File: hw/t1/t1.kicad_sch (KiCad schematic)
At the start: 62 parts, among them J1 SFP edge (INF-8074i), J2 H-MTD 1-port PCB header - FOO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, U1 DP83TG720S-Q1 (or DP83TC812S-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, U2 STM32G031F6P6, U3 TPS62821DLC, Y1 25MHz CL8pF 2016

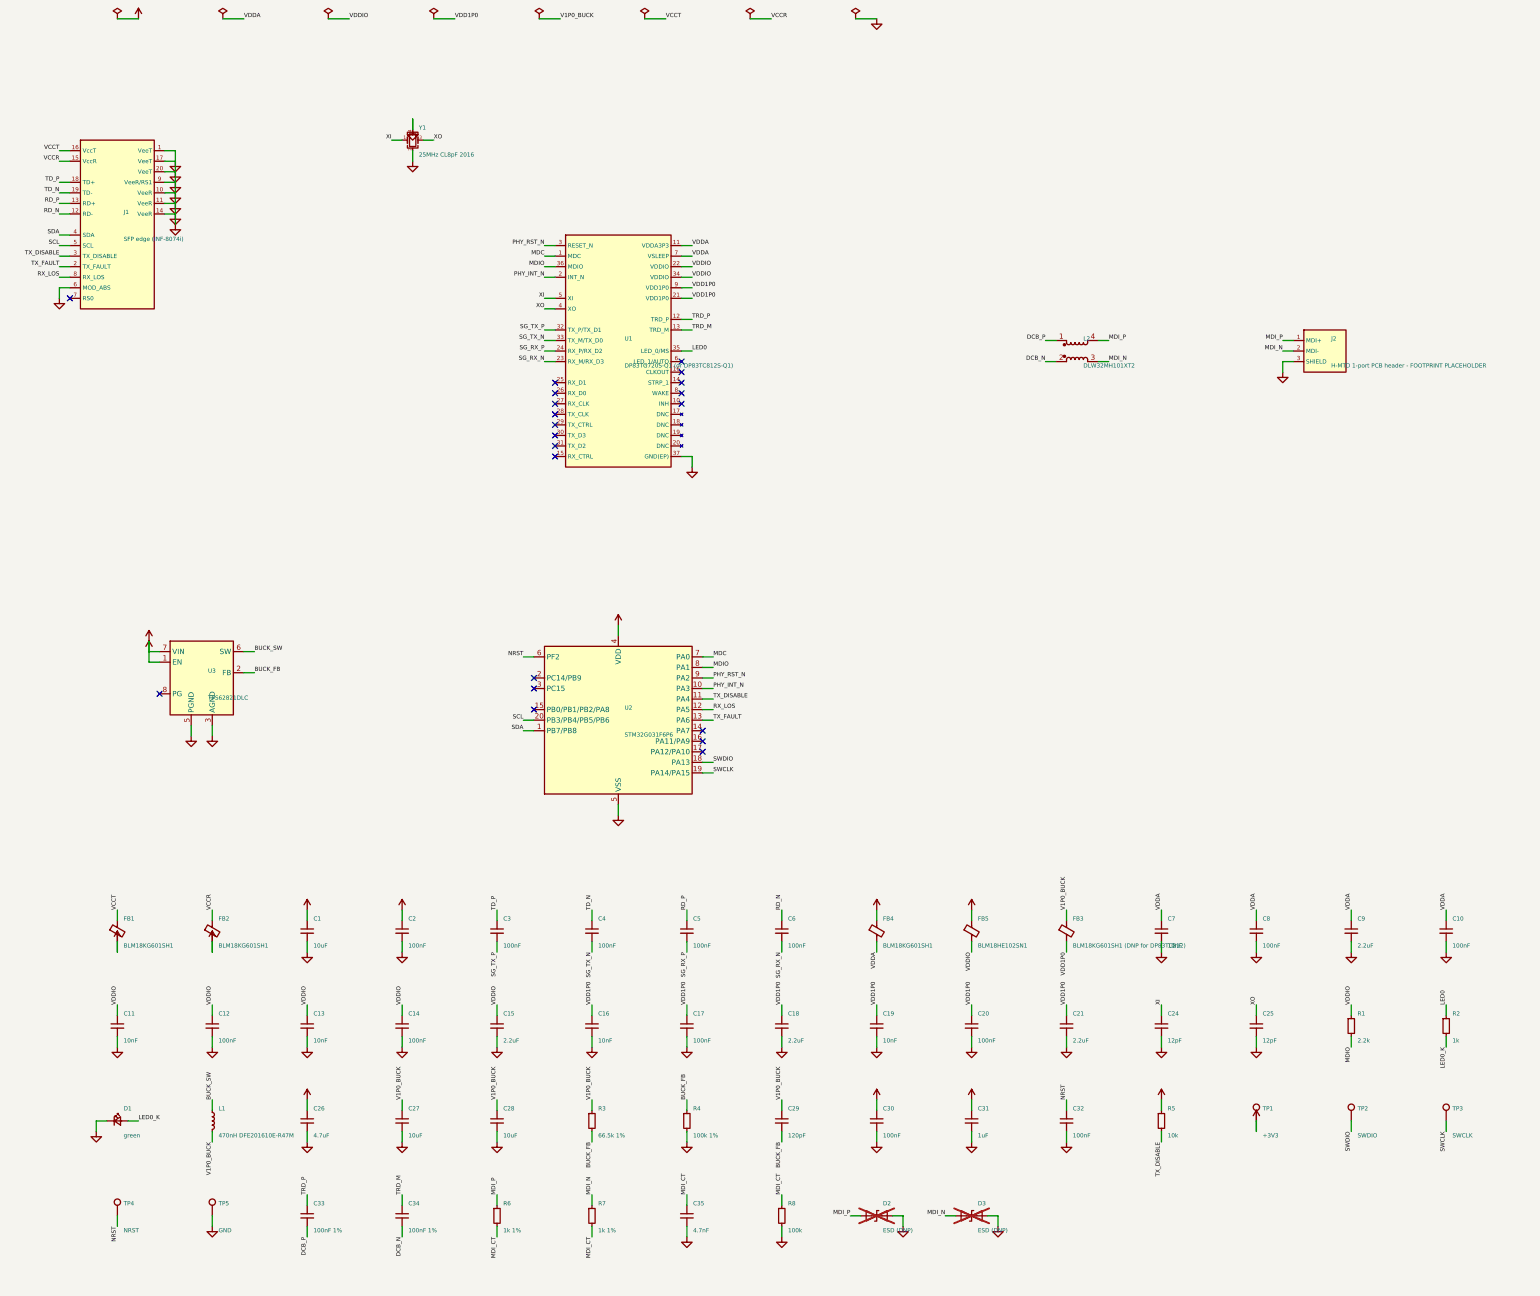
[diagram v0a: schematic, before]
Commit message: T1: orderable at JLC - real H-MTD land, JLC 3313 widths, panel, BOM/CPL with LCSC
J2 is now the Rosenberger E6S20A-40MT5-Z land from layout drawing MB_633:
ground holes 7.0 x 7.5 (9.3 is the hatched-area width, not the pitch),
signal pair 2.0 apart 1.87 behind the front row, its solder areas and
no-routing keep-outs. The body sits past the cage front, so the board
grows to 63.5 mm.

Widths from JLC04101H-3313 (50 ohm single-ended 0.157 mm); pair skew at
most 2.0 mm. TPS62822 replaces the out-of-stock TPS62821. Every assembled
part carries its LCSC number in schematic and PCB.

panel_t1.py: 5 boards, mouse bites, rails on three sides so the finger
edge stays a clean bevel edge (panel_rails.py, a KiKit framing plugin);
70.6 x 81.1 mm; panel DRC 0 errors; 265 unique placements.
Routed board: DRC 0 / unconnected 0, ERC 0.
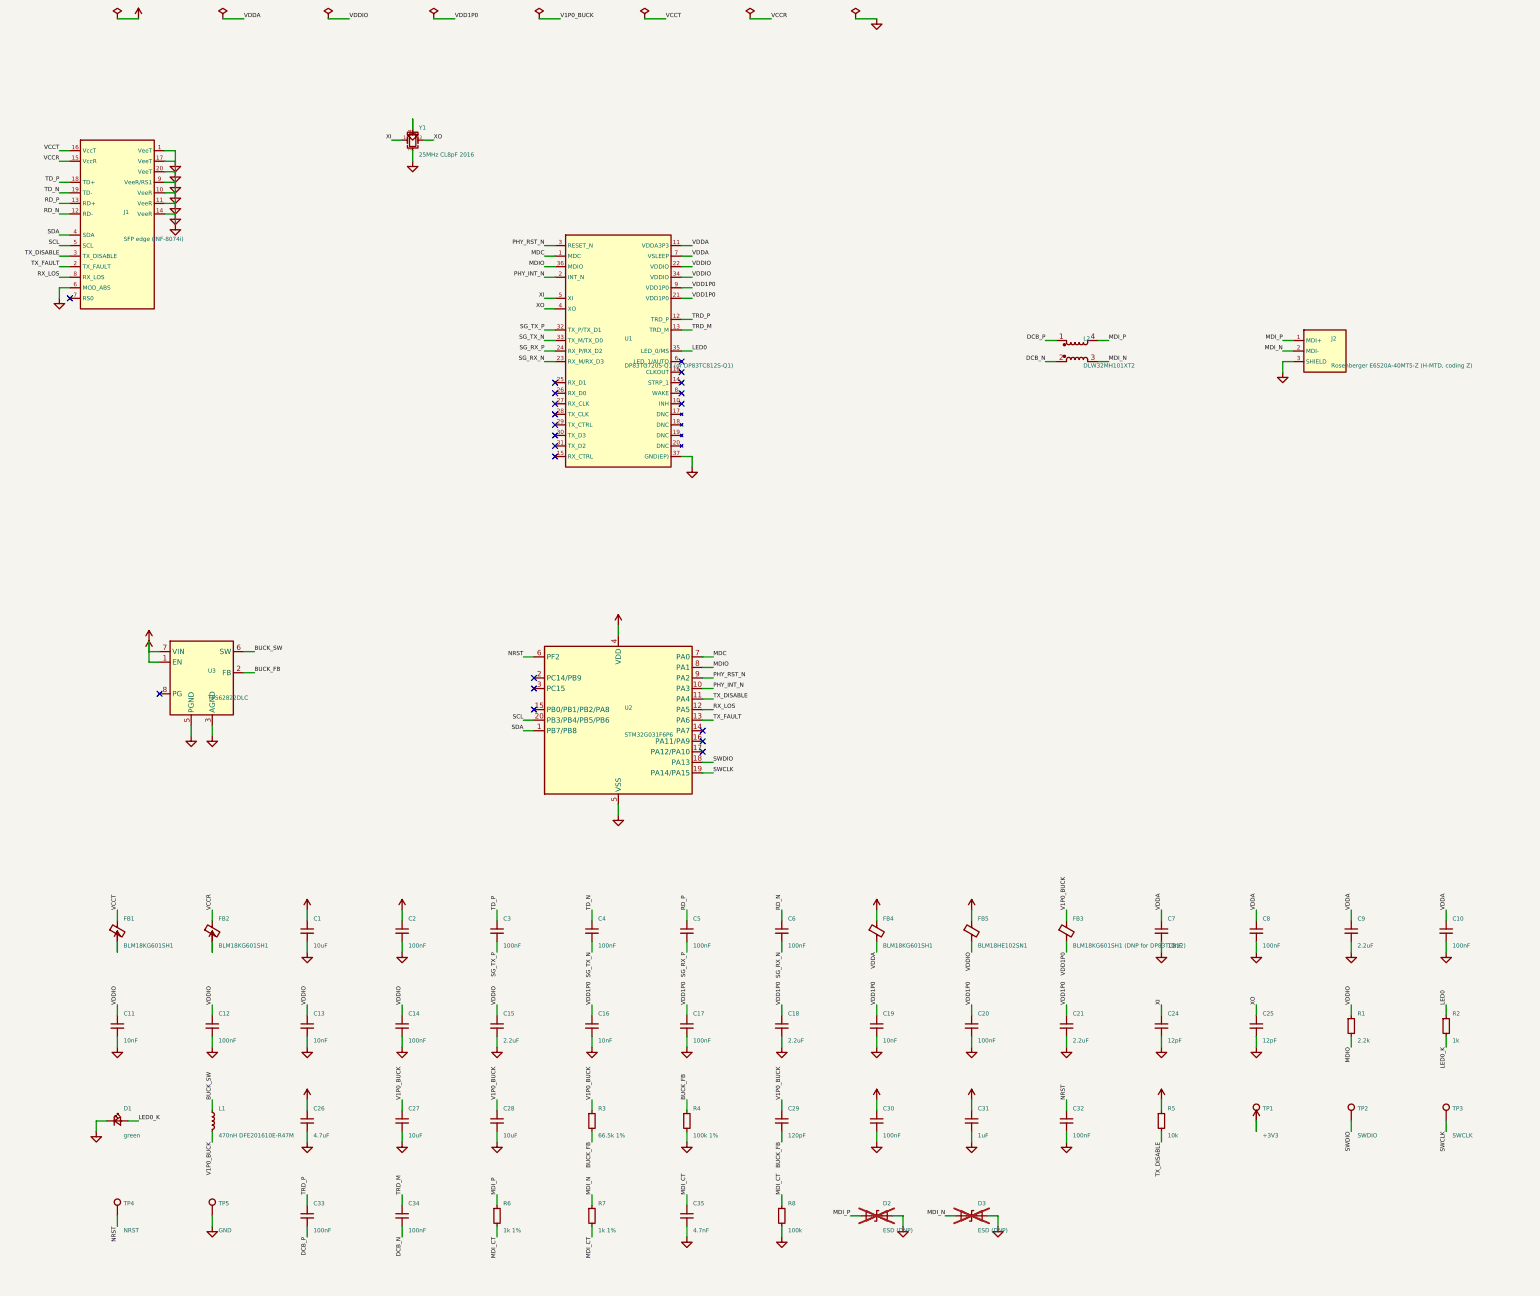
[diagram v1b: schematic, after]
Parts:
- C1, C27, C28: LCSC (none) -> C19702
- C10, C12, C14, C17, C20, C3, C4, C5, C6, C8: LCSC (none) -> C76928
- C11, C13, C16, C19, C7: LCSC (none) -> C285010
- C15, C18, C21, C9: LCSC (none) -> C12530
- C2, C30, C32: LCSC (none) -> C1525
- C24, C25: LCSC (none) -> C50391
- C26: LCSC (none) -> C23733
- C29: LCSC (none) -> C161406
- C31: LCSC (none) -> C52923
- C33, C34: value 100nF 1% -> 100nF; LCSC (none) -> C1525
- C35: LCSC (none) -> C1538
- D1: LCSC (none) -> C965793
- FB1, FB2, FB3, FB4: LCSC (none) -> C710379
- FB5: LCSC (none) -> C85828
- J2: value H-MTD 1-port PCB header - FOOTPRINT PLACEHOLDER -> Rosenberger E6S20A-40MT5-Z (H-MTD, coding Z); footprint sfp:HMTD_1P_Placeholder -> sfp:Rosenberger_HMTD_E6S20A_1P_RA; MPN (none) -> E6S20A-40MT5-Z
- L1: LCSC (none) -> C269773
- L2: LCSC (none) -> C2935101
- R1: LCSC (none) -> C142018
- R2: LCSC (none) -> C11702
- R3: LCSC (none) -> C62193
- R4: LCSC (none) -> C106224
- R5: LCSC (none) -> C25744
- R6, R7: LCSC (none) -> C21190
- R8: LCSC (none) -> C25741
- U1: LCSC (none) -> C2921292
- U2: LCSC (none) -> C529333
- U3: value TPS62821DLC -> TPS62822DLC; LCSC (none) -> C473385; MPN TPS62821DLCR -> TPS62822DLCR
- Y1: LCSC (none) -> C7301943

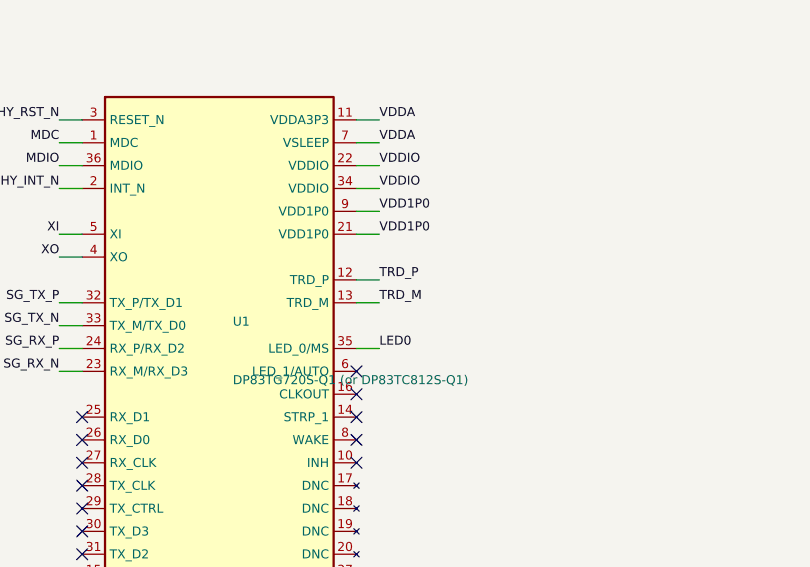
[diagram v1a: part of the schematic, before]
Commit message: t1: routed DRC-clean with the pairs on F/B only, panel clean
- In2's +3V3 pour goes in after routing: in the DSN it made +3V3 a plane
  net the router never routed, while signals cut the plane up
- SGMII/MDI classes restricted to F and B (use_layer): the router had
  split pairs P-on-B / N-on-In2. U1 pins 12/13 cross over on purpose;
  the PHY corrects MDI polarity itself (datasheet 6.4.7.2)
- placement: Y1 turned 180 so XI/XO face pins 5/4 uncrossed, load caps
  underneath; buck rearranged (divider by FB, input cap under VIN, EN to
  VIN under the package); SWD test points moved off the crystal
- locked pre-routes and escape vias where the router kept failing,
  cap dogbones, then post-route repair: unused escape vias out, open
  links joined before GND stitching, vias into ground islands
- panel: mouse bites 0.1 mm into the board, stitching 1 mm off the long
  edges, bottom label off the edge; panel DRC 0 errors
- ERC 0/0, DRC 0 violations 0 unconnected, pair skew <= 3.2 mm
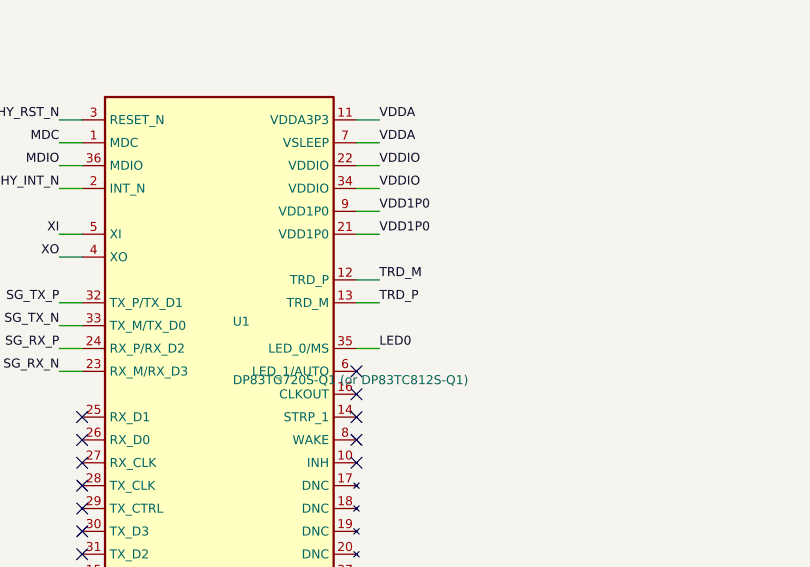
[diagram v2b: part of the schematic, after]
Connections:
- net TRD_M: now also U1.12 (TRD_P); no longer U1.13 (TRD_M)
- net TRD_P: now also U1.13 (TRD_M); no longer U1.12 (TRD_P)
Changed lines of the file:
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@@
   (label "VDD1P0" (at 177.80 97.79 0) (effects (font (size 1.0 1.0)) (justify left bottom)))
   (wire (pts (xy 175.26 102.87) (xy 177.80 102.87)) (stroke (width 0) (type default)))
-  (label "TRD_P" (at 177.80 102.87 0) (effects (font (size 1.0 1.0)) (justify left bottom)))
+  (label "TRD_M" (at 177.80 102.87 0) (effects (font (size 1.0 1.0)) (justify left bottom)))
   (wire (pts (xy 175.26 105.41) (xy 177.80 105.41)) (stroke (width 0) (type default)))
-  (label "TRD_M" (at 177.80 105.41 0) (effects (font (size 1.0 1.0)) (justify left bottom)))
+  (label "TRD_P" (at 177.80 105.41 0) (effects (font (size 1.0 1.0)) (justify left bottom)))
   (wire (pts (xy 175.26 110.49) (xy 177.80 110.49)) (stroke (width 0) (type default)))
   (label "LED0" (at 177.80 110.49 0) (effects (font (size 1.0 1.0)) (justify left bottom)))
